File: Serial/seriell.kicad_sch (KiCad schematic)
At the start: 27 parts, among them J1 Conn_01x10_Pin, J10 Conn_01x06, J11 Conn_01x06, J12 TTL, J13 Conn_01x10_Pin, J14 Conn_01x10_Pin, J15 Conn_01x10_Pin, J16 Conn_01x10_Pin, J17 Conn_01x10_Pin, J18 Conn_01x10_Pin, J19 Bluetooth, J2 Conn_01x10_Pin, J20 Conn_01x04, J3 Conn_01x10_Pin, J30 Flash, J4 Conn_01x10_Pin, J5 Conn_01x10_Pin, J6 Conn_01x10_Pin, J7 Conn_02x04_Counter_Clockwise, J8 BT

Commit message: flash
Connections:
- net GND: now also J1.10 (Pin_10), J10.2 (Pin_2), J11.6 (Pin_6), J12.1 (Pin_1), J13.10 (Pin_10), J20.1 (Pin_1), J8.3 (Pin_3)

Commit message: serial redesign
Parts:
- removed J19: Bluetooth, Connector_PinHeader_2.54mm:PinHeader_1x02_P2.54mm_Vertical, symbol Connector:Conn_01x02_Pin
- removed J30: Flash, Connector_PinHeader_2.54mm:PinHeader_2x03_P2.54mm_Vertical, symbol Connector_Generic:Conn_02x03_Counter_Clockwise
- added JP1: Bluetooth, Jumper:SolderJumper-2_P1.3mm_Open_Pad1.0x1.5mm, symbol Jumper:Jumper_2_Open
- added JP2: RX, Jumper:SolderJumper-2_P1.3mm_Open_Pad1.0x1.5mm, symbol Jumper:Jumper_2_Open
- added JP3: TX, Jumper:SolderJumper-2_P1.3mm_Open_Pad1.0x1.5mm, symbol Jumper:Jumper_2_Open
- J20: value Conn_01x04 -> Auslesen
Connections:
- net TX: now reaches J10.3 (Pin_3), J11.3 (Pin_3), J12.3 (Pin_3), J15.7 (Pin_7), J20.3 (Pin_3), J3.7 (Pin_7), J8.2 (Pin_2)
- net TX: now also JP3.1 (A)
- net RX: now reaches J10.4 (Pin_4), J11.2 (Pin_2), J12.2 (Pin_2), J14.8 (Pin_8), J2.8 (Pin_8), J20.2 (Pin_2)
- net RX: now also J8.1 (Pin_1), JP2.1 (A)
- net at J10.1 (Pin_1): no longer J10.5 (Pin_5)
- net +5V: now reaches J1.1 (Pin_1), J13.1 (Pin_1), J20.4 (Pin_4)
- net +5V: now also JP1.1 (A)
- net at J8.4 (Pin_4): now also JP1.2 (B)
- net at A1.1 (D1/TX): now also JP3.2 (B)
- net at A1.2 (D0/RX): now also JP2.2 (B)
- no-connect marks 28 -> 27
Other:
- moved on the sheet: A1

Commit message: wemos
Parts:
- added U1: WeMos_D1_mini, Module:WEMOS_D1_mini_light, symbol MCU_Module:WeMos_D1_mini
- D2: value Error -> Fehler
- D3: value Power -> Bereit
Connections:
- net GND: now also U1.10 (GND)
- net at A1.12 (D9), D3.2 (A): now also U1.3 (D0)
- net at JP3.2 (B): now also U1.16 (TX); no longer A1.1 (D1/TX)
- net at JP2.2 (B): now also U1.15 (RX); no longer A1.2 (D0/RX)
- net at A1.11 (D8), D2.2 (A): now also U1.12 (D3)
- net at A1.10 (D7), D1.2 (A): now also U1.11 (D4)
- net CS: now reaches A1.13 (D10), J7.3 (Pin_3)
- net CS: now also U1.7 (CS/D8)
- net MOSI: now reaches A1.14 (D11), J7.4 (Pin_4)
- net MOSI: now also U1.6 (MOSI/D7)
- net MISO: now reaches A1.15 (D12), J7.5 (Pin_5)
- net MISO: now also U1.5 (MISO/D6)
- net SCK: now reaches A1.16 (D13), J7.6 (Pin_6)
- net SCK: now also U1.4 (SCK/D5)
- net +3.3V: now reaches A1.17 (3V3), J7.7 (Pin_7)
- net +3.3V: now also U1.8 (3V3)
- net +5VA: now reaches A1.27 (+5V), J7.2 (Pin_2)
- net +5VA: now also U1.9 (5V)
- no-connect marks 27 -> 33
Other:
- moved on the sheet: D1, D2, D3, J1, J10, J11, J12, J13, J14, J15, J16, J17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

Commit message: esp
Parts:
- removed A1: Arduino_Nano_v3.x, Module:Arduino_Nano, symbol MCU_Module:Arduino_Nano_v3.x
- removed J1, J13, J14, J15, J16, J17, J18, J2, J3, J4, J5, J6: Conn_01x10_Pin, Connector_PinSocket_2.54mm:PinSocket_1x10_P2.54mm_Vertical, symbol Connector:Conn_01x10_Pin
- removed J10, J11: Conn_01x06, Connector_PinHeader_2.54mm:PinHeader_1x06_P2.54mm_Vertical, symbol Connector_Generic:Conn_01x06
- removed J12: TTL, Connector_PinHeader_2.54mm:PinHeader_1x06_P2.54mm_Vertical, symbol Connector_Generic:Conn_01x06
- removed J20: Auslesen, Connector_PinHeader_2.54mm:PinHeader_1x04_P2.54mm_Vertical, symbol Connector_Generic:Conn_01x04
- removed J8: BT, Connector_PinHeader_2.54mm:PinHeader_1x04_P2.54mm_Vertical, symbol Connector_Generic:Conn_01x04
- removed JP1: Bluetooth, Jumper:SolderJumper-2_P1.3mm_Open_Pad1.0x1.5mm, symbol Jumper:Jumper_2_Open
- removed JP2: RX, Jumper:SolderJumper-2_P1.3mm_Open_Pad1.0x1.5mm, symbol Jumper:Jumper_2_Open
- removed JP3: TX, Jumper:SolderJumper-2_P1.3mm_Open_Pad1.0x1.5mm, symbol Jumper:Jumper_2_Open
- removed U1: WeMos_D1_mini, Module:WEMOS_D1_mini_light, symbol MCU_Module:WeMos_D1_mini
- added C1, C2: 10uF, Capacitor_SMD:C_0603_1608Metric, symbol Device:C
- added D4: D, Diode_SMD:D_SOD-123, symbol Device:D
- added J1, J3: Datenbank, Connector_DIN:DIN41612_C3_3x10_Female_Vertical_THT, symbol DIN41612:DIN41612_03x10_ABC
- added J2, J4: Steuereinheit, Connector_DIN:DIN41612_R3_3x10_Male_Vertical_THT, symbol DIN41612:DIN41612_03x10_ABC
- added P1: USB_C_Plug_USB2.0, Connector_USB:USB_C_Receptacle_G-Switch_GT-USB-7010ASV, symbol Connector:USB_C_Plug_USB2.0
- added U1: ESP32-C3-WROOM-02, RF_Module:ESP32-C3-WROOM-02, symbol RF_Module:ESP32-C3-WROOM-02
- added U2: AMS1117-3.3, Package_TO_SOT_SMD:SOT-223-3_TabPin2, symbol Regulator_Linear:AMS1117-3.3
- D1, D2, D3: footprint LED_THT:LED_D5.0mm -> LED_SMD:LED_0603_1608Metric
- J7: footprint Connector_PinHeader_2.54mm:PinHeader_2x04_P2.54mm_Vertical -> Connector_IDC:IDC-Header_2x04_P2.54mm_Vertical
- R1, R2, R3: footprint Resistor_SMD:R_0805_2012Metric -> LED_SMD:LED_0603_1608Metric
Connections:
- net +3.3V: now also C1.1, U1.1 (3V3), U2.2 (VO)
- net +5V: now also D4.2 (A), J1.a1 (Pin_a1), J2.a10 (Pin_a10)
- net +5VA: now also C2.1, D4.1 (K), U2.3 (VI)
- net CS: now also U1.6 (IO7)
- net GND: now also C1.2, C2.2, J1.a10 (Pin_a10), J1.a4 (Pin_a4), J2.a1 (Pin_a1), J2.a7 (Pin_a7), J3.a10 (Pin_a10), J3.a4 (Pin_a4), J4.a1 (Pin_a1), J4.a7 (Pin_a7), P1.A1 (GND), P1.A12 (GND), P1.B1 (GND), P1.B12 (GND), P1.S1 (SHIELD), U1.19 (GND), U1.9 (GND), U2.1 (GND)
- net MISO: now also U1.8 (IO9)
- net MOSI: now also U1.7 (IO8)
- net RX: now also J1.b8 (Pin_b8), J2.b3 (Pin_b3), U1.11 (IO20/RXD)
- net SCK: now also U1.10 (IO10)
- net TX: now also J1.c7 (Pin_c7), J2.c4 (Pin_c4), U1.12 (IO21/TXD)
- net at D3.2 (A): now also U1.15 (IO3)
- net at D2.2 (A): now also U1.16 (IO2)
- net at D1.2 (A): now also U1.17 (IO1)
- new net: J1.c10 (Pin_c10), J2.c1 (Pin_c1)
- new net: J1.c1 (Pin_c1), J2.c10 (Pin_c10)
- new net: J1.c9 (Pin_c9), J2.c2 (Pin_c2)
- new net: J1.c8 (Pin_c8), J2.c3 (Pin_c3)
- new net: J1.c6 (Pin_c6), J2.c5 (Pin_c5)
- new net: J1.c5 (Pin_c5), J2.c6 (Pin_c6)
- new net: J1.c4 (Pin_c4), J2.c7 (Pin_c7)
- new net: J1.c3 (Pin_c3), J2.c8 (Pin_c8)
- new net: J1.c2 (Pin_c2), J2.c9 (Pin_c9)
- new net: J3.a1 (Pin_a1), J4.a10 (Pin_a10)
- new net: J3.a9 (Pin_a9), J4.a2 (Pin_a2)
- new net: J3.a8 (Pin_a8), J4.a3 (Pin_a3)
- new net: J3.a7 (Pin_a7), J4.a4 (Pin_a4)
- new net: J3.a6 (Pin_a6), J4.a5 (Pin_a5)
- new net: J3.a5 (Pin_a5), J4.a6 (Pin_a6)
- new net: J3.a3 (Pin_a3), J4.a8 (Pin_a8)
- new net: J3.a2 (Pin_a2), J4.a9 (Pin_a9)
- new net: J3.c1 (Pin_c1), J4.c10 (Pin_c10)
- new net: J3.c10 (Pin_c10), J4.c1 (Pin_c1)
- new net: J3.c2 (Pin_c2), J4.c9 (Pin_c9)
- new net: J3.c3 (Pin_c3), J4.c8 (Pin_c8)
- new net: J3.c4 (Pin_c4), J4.c7 (Pin_c7)
- new net: J3.c5 (Pin_c5), J4.c6 (Pin_c6)
- new net: J3.c6 (Pin_c6), J4.c5 (Pin_c5)
- new net: J3.c7 (Pin_c7), J4.c4 (Pin_c4)
- new net: J3.c8 (Pin_c8), J4.c3 (Pin_c3)
- new net: J3.c9 (Pin_c9), J4.c2 (Pin_c2)
- new net: J1.b10 (Pin_b10), J2.b1 (Pin_b1)
- new net: J1.b1 (Pin_b1), J2.b10 (Pin_b10)
- new net: J1.b9 (Pin_b9), J2.b2 (Pin_b2)
- new net: J1.b7 (Pin_b7), J2.b4 (Pin_b4)
- new net: J1.b6 (Pin_b6), J2.b5 (Pin_b5)
- new net: J1.b5 (Pin_b5), J2.b6 (Pin_b6)
- new net: J1.b4 (Pin_b4), J2.b7 (Pin_b7)
- new net: J1.b3 (Pin_b3), J2.b8 (Pin_b8)
- new net: J1.b2 (Pin_b2), J2.b9 (Pin_b9)
- new net: J3.b1 (Pin_b1), J4.b10 (Pin_b10)
- new net: J3.b10 (Pin_b10), J4.b1 (Pin_b1)
- new net: J3.b2 (Pin_b2), J4.b9 (Pin_b9)
- new net: J3.b3 (Pin_b3), J4.b8 (Pin_b8)
- new net: J3.b4 (Pin_b4), J4.b7 (Pin_b7)
- new net: J3.b5 (Pin_b5), J4.b6 (Pin_b6)
- new net: J3.b6 (Pin_b6), J4.b5 (Pin_b5)
- new net: J3.b7 (Pin_b7), J4.b4 (Pin_b4)
- new net: J3.b8 (Pin_b8), J4.b3 (Pin_b3)
- new net: J3.b9 (Pin_b9), J4.b2 (Pin_b2)
- new net: P1.A7 (D-), U1.13 (IO18)
- new net: P1.A6 (D+), U1.14 (IO19)
- new net: J1.a9 (Pin_a9), J2.a2 (Pin_a2)
- new net: J1.a8 (Pin_a8), J2.a3 (Pin_a3)
- new net: J1.a7 (Pin_a7), J2.a4 (Pin_a4)
- new net: J1.a6 (Pin_a6), J2.a5 (Pin_a5)
- new net: J1.a5 (Pin_a5), J2.a6 (Pin_a6)
- new net: J1.a3 (Pin_a3), J2.a8 (Pin_a8)
- new net: J1.a2 (Pin_a2), J2.a9 (Pin_a9)
- new net VBUS: P1.A4 (VBUS), P1.A9 (VBUS), P1.B4 (VBUS), P1.B9 (VBUS)
- no-connect marks 33 -> 1
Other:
- moved on the sheet: D1, D2, D3, J7, R1, R2, R3

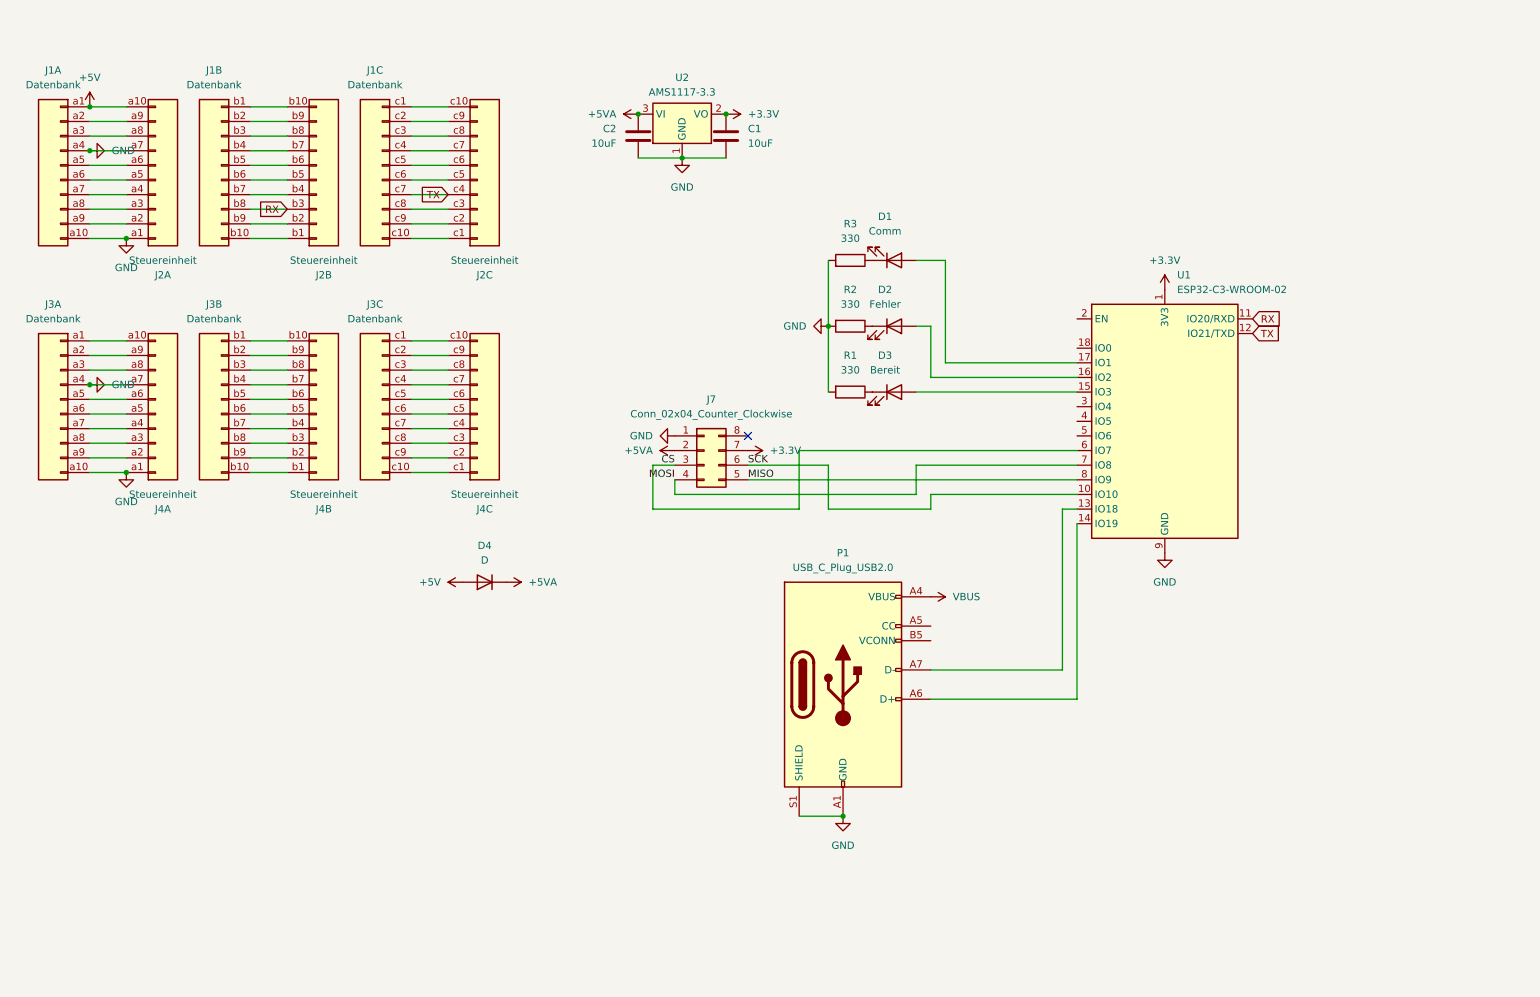
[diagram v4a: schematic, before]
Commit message: usbasp stecker
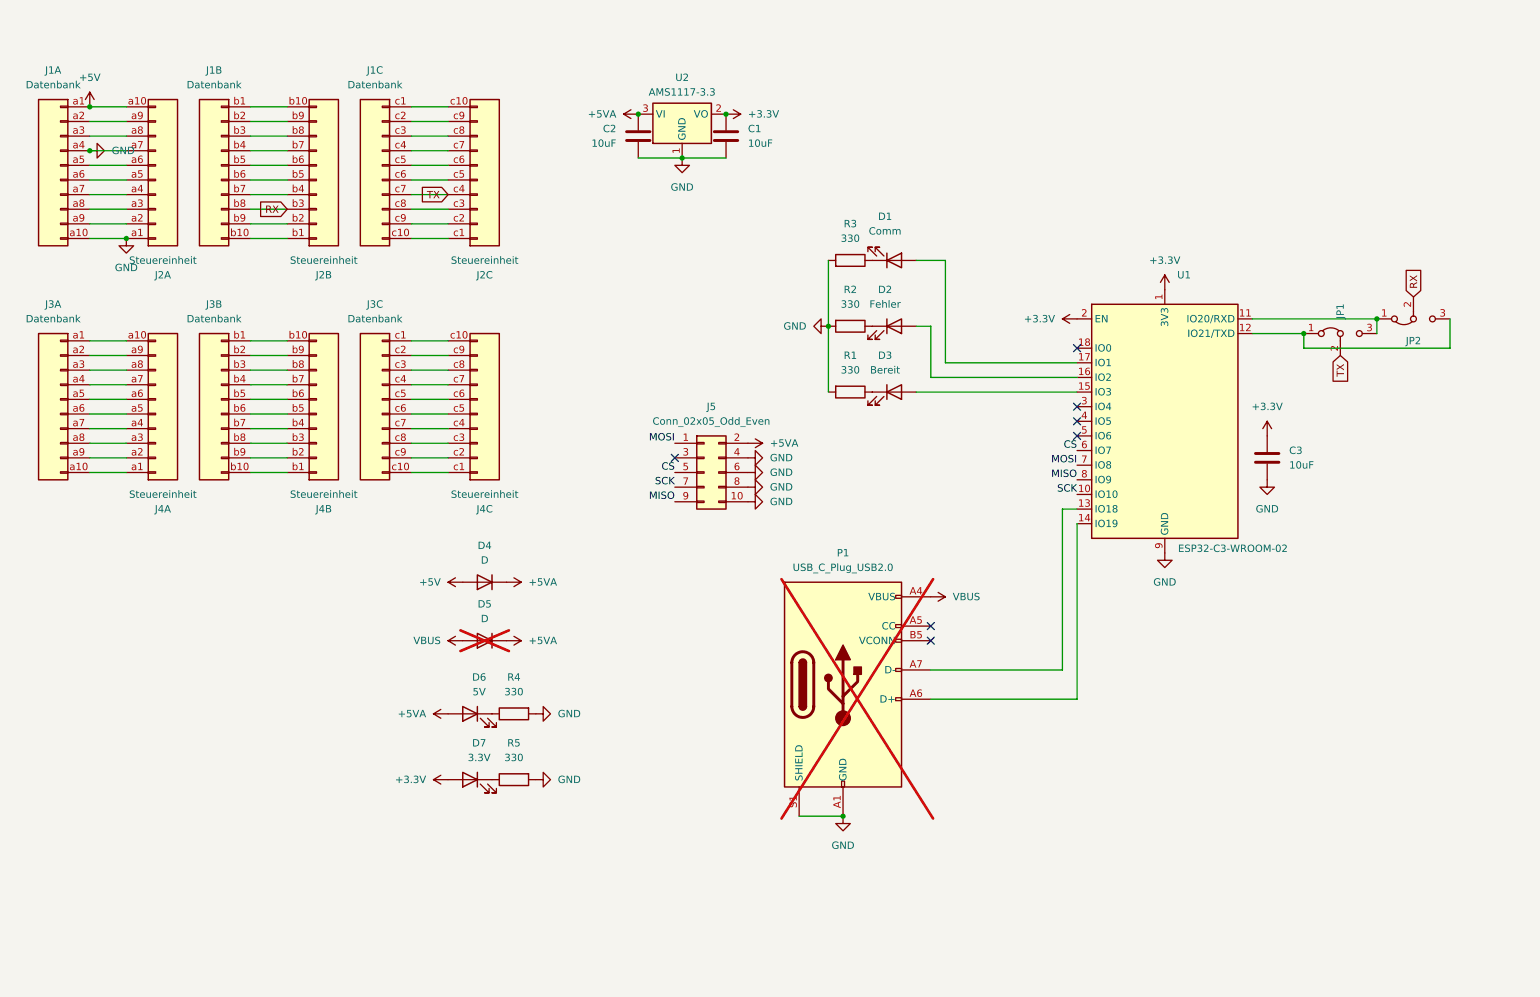
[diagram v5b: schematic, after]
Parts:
- removed J7: Conn_02x04_Counter_Clockwise, Connector_IDC:IDC-Header_2x04_P2.54mm_Vertical, symbol Connector_Generic:Conn_02x04_Counter_Clockwise
- added C3: 10uF, Capacitor_SMD:C_0603_1608Metric, symbol Device:C
- added D5: D, Diode_SMD:D_SOD-123, symbol Device:D
- added D6: 5V, LED_SMD:LED_0603_1608Metric, symbol Device:LED
- added D7: 3.3V, LED_SMD:LED_0603_1608Metric, symbol Device:LED
- added J5: Conn_02x05_Odd_Even, Connector_IDC:IDC-Header_2x05_P2.54mm_Vertical, symbol Connector_Generic:Conn_02x05_Odd_Even
- added JP1: TX, Jumper:SolderJumper-3_P1.3mm_Bridged2Bar12_Pad1.0x1.5mm, symbol Jumper:Jumper_3_Bridged12
- added JP2: RX, Jumper:SolderJumper-3_P1.3mm_Bridged2Bar12_Pad1.0x1.5mm, symbol Jumper:Jumper_3_Bridged12
- added R4, R5: 330, LED_SMD:LED_0603_1608Metric, symbol Device:R
- P1: now not fitted
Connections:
- net +3.3V: now also U1.2 (EN), C3.1, D7.2 (A)
- net +5VA: now also D5.1 (K), D6.2 (A), J5.2 (Pin_2)
- net CS: now also J5.5 (Pin_5)
- net GND: now also C3.2, J5.10 (Pin_10), J5.4 (Pin_4), J5.6 (Pin_6), J5.8 (Pin_8), R4.2, R5.2; no longer J3.a10 (Pin_a10), J3.a4 (Pin_a4), J4.a1 (Pin_a1), J4.a7 (Pin_a7)
- net MISO: now also J5.9 (Pin_9)
- net MOSI: now also J5.1 (Pin_1)
- net RX: now also JP2.2 (C); no longer U1.11 (IO20/RXD)
- net SCK: now also J5.7 (Pin_7)
- net TX: now also JP1.2 (C); no longer U1.12 (IO21/TXD)
- net VBUS: now also D5.2 (A)
- new net: J3.a10 (Pin_a10), J4.a1 (Pin_a1)
- new net: J3.a4 (Pin_a4), J4.a7 (Pin_a7)
- new net: D6.1 (K), R4.1
- new net: JP1.3 (B), JP2.1 (A), U1.11 (IO20/RXD)
- new net: JP1.1 (A), JP2.3 (B), U1.12 (IO21/TXD)
- new net: D7.1 (K), R5.1
- no-connect marks 1 -> 7
